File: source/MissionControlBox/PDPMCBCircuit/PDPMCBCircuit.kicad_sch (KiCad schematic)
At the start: 63 parts

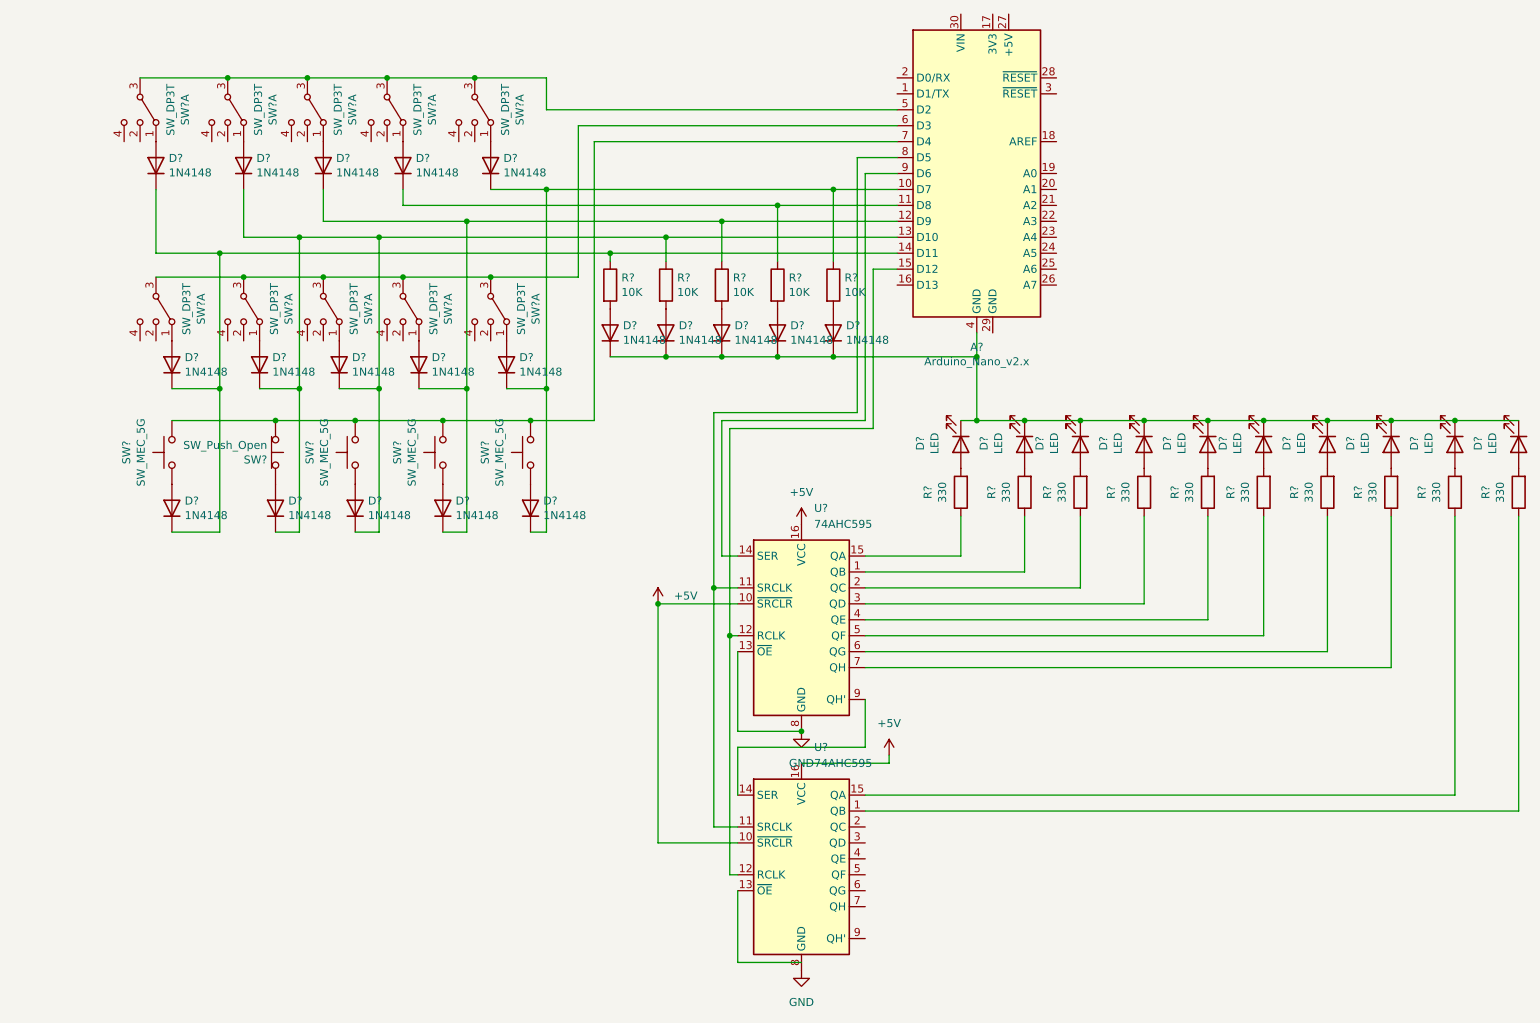
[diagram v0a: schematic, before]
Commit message: Added Labels to circuit
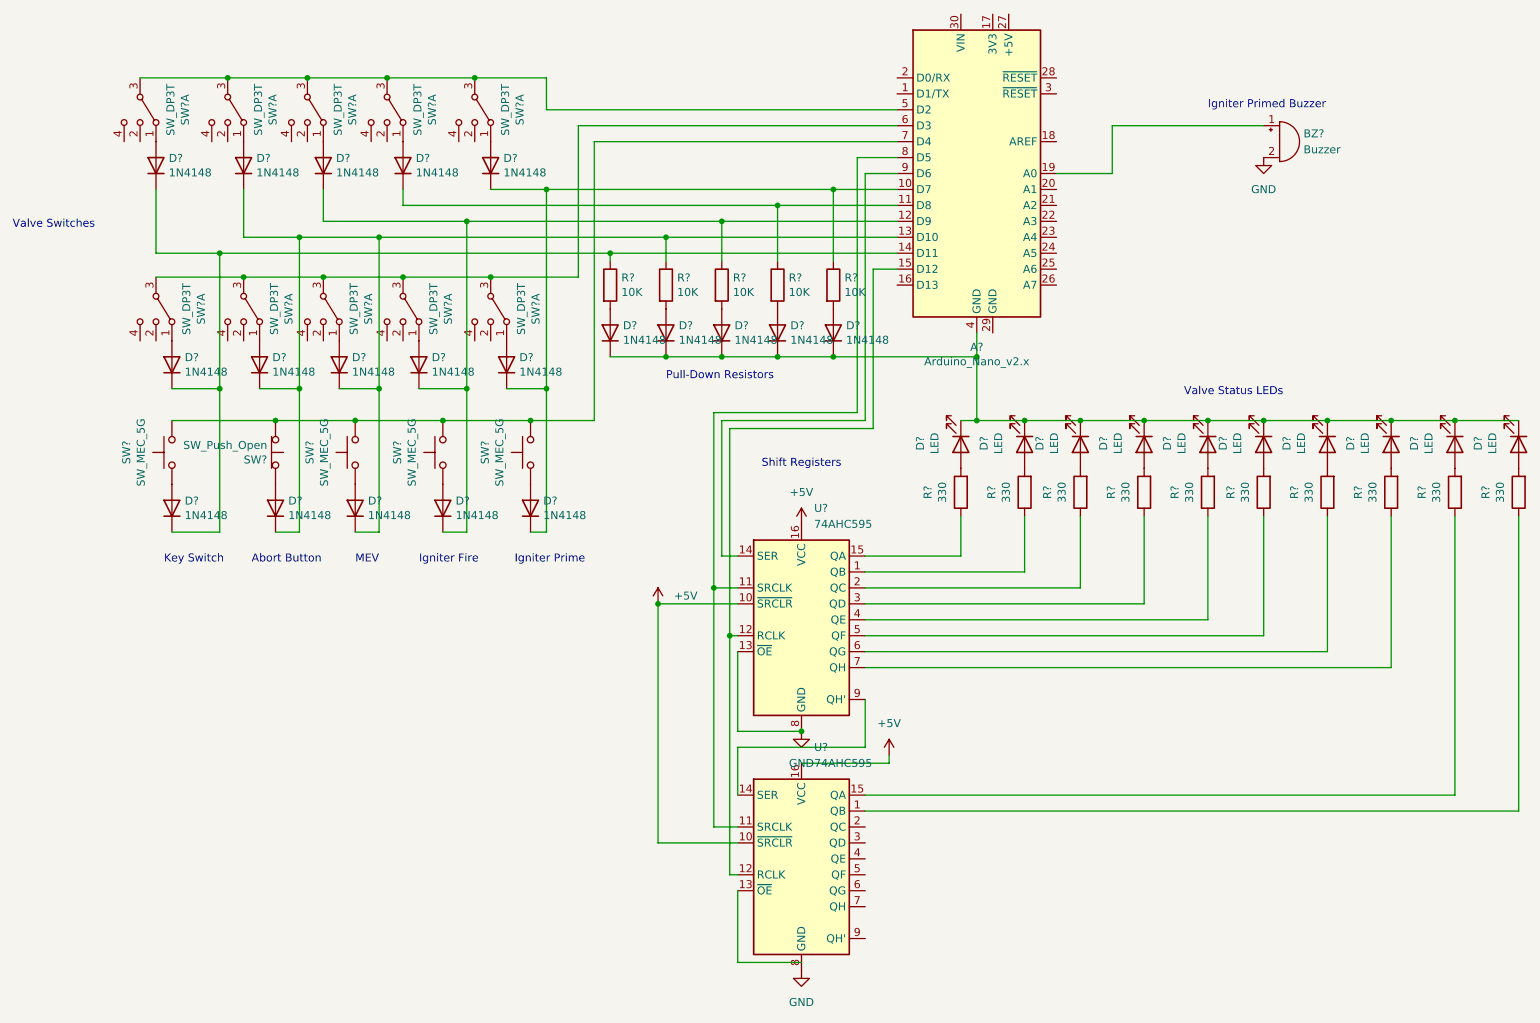
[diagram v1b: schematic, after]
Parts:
- added BZ?: Buzzer, symbol Device:Buzzer
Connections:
- net GND: now also BZ?.2 (+)
- net at A?.19 (A0): now also BZ?.1 (-)
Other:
- note added: "Abort Button"
- note added: "Igniter Fire"
- note added: "Igniter Prime"
- note added: "Igniter Primed Buzzer"
- note added: "Key Switch"
- note added: "MEV"
- note added: "Pull-Down Resistors"
- note added: "Shift Registers"
- note added: "Valve Status LEDs"
- note added: "Valve Switches"
- company: (none) -> UVic Rocketery
- title: (none) -> Propulsion Developement Platform Mission Control Box
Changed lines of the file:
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@@
 (kicad_sch (version 20211123) (generator eeschema)
   (paper "A4")
+  (title_block
+    (title "Propulsion Developement Platform Mission Control Box")
+    (date "2022-05-11")
+    (rev "R1")
+    (company "UVic Rocketery")
+  )
   (junction (at 100.33 60.96) (diameter 0) (color 0 0 0 0)
   )
@@
     (stroke (width 0) (type default) (color 0 0 0 0))
   )
+  (wire (pts (xy 203.2 53.34) (xy 203.2 45.72))
+    (stroke (width 0) (type default) (color 0 0 0 0))
+  )
   (wire (pts (xy 104.14 69.85) (xy 118.11 69.85))
     (stroke (width 0) (type default) (color 0 0 0 0))
@@
     (stroke (width 0) (type default) (color 0 0 0 0))
   )
+  (wire (pts (xy 203.2 45.72) (xy 227.33 45.72))
+    (stroke (width 0) (type default) (color 0 0 0 0))
+  )
   (wire (pts (xy 60.96 110.49) (xy 60.96 87.63))
     (stroke (width 0) (type default) (color 0 0 0 0))
@@
     (stroke (width 0) (type default) (color 0 0 0 0))
   )
+  (wire (pts (xy 194.31 53.34) (xy 203.2 53.34))
+    (stroke (width 0) (type default) (color 0 0 0 0))
+  )
   (wire (pts (xy 106.68 87.63) (xy 113.03 87.63))
     (stroke (width 0) (type default) (color 0 0 0 0))
@@
   (wire (pts (xy 247.65 92.71) (xy 237.49 92.71))
     (stroke (width 0) (type default) (color 0 0 0 0))
+  )
+  (text "Valve Switches\n" (at 27.94 62.23 0)
+    (effects (font (size 1.27 1.27)) (justify left bottom))
+  )
+  (text "MEV\n" (at 82.55 115.57 0)
+    (effects (font (size 1.27 1.27)) (justify left bottom))
+  )
+  (text "Shift Registers" (at 147.32 100.33 0)
+    (effects (font (size 1.27 1.27)) (justify left bottom))
+  )
+  (text "Abort Button" (at 66.04 115.57 0)
+    (effects (font (size 1.27 1.27)) (justify left bottom))
+  )
+  (text "Igniter Prime\n" (at 107.95 115.57 0)
+    (effects (font (size 1.27 1.27)) (justify left bottom))
+  )
+  (text "Key Switch\n" (at 52.07 115.57 0)
+    (effects (font (size 1.27 1.27)) (justify left bottom))
+  )
+  (text "Valve Status LEDs" (at 214.63 88.9 0)
+    (effects (font (size 1.27 1.27)) (justify left bottom))
+  )
+  (text "Igniter Fire\n" (at 92.71 115.57 0)
+    (effects (font (size 1.27 1.27)) (justify left bottom))
+  )
+  (text "Pull-Down Resistors" (at 132.08 86.36 0)
+    (effects (font (size 1.27 1.27)) (justify left bottom))
+  )
+  (text "Igniter Primed Buzzer" (at 218.44 43.18 0)
+    (effects (font (size 1.27 1.27)) (justify left bottom))
   )
   (symbol (lib_id "MCU_Module:Arduino_Nano_v2.x") (at 181.61 53.34 0) (unit 1)
@@
     (pin "1")
   )
+  (symbol (lib_id "Device:Buzzer") (at 229.87 48.26 0) (unit 1)
+    (in_bom yes) (on_board yes) (fields_autoplaced)
+    (property "Reference" "BZ?" (id 0) (at 233.68 46.9899 0)
+      (effects (font (size 1.27 1.27)) (justify left))
+    )
+    (property "Value" "Buzzer" (id 1) (at 233.68 49.5299 0)
+      (effects (font (size 1.27 1.27)) (justify left))
+    )
+    (property "Footprint" "" (id 2) (at 229.235 45.72 90)
+      (effects (font (size 1.27 1.27)) hide)
+    )
+    (property "Datasheet" "~" (id 3) (at 229.235 45.72 90)
+      (effects (font (size 1.27 1.27)) hide)
+    )
+    (pin "1")
+    (pin "2")
+  )
+  (symbol (lib_id "power:GND") (at 227.33 50.8 0) (unit 1)
+    (in_bom yes) (on_board yes) (fields_autoplaced)
+    (property "Reference" "#PWR?" (id 0) (at 227.33 57.15 0)
+      (effects (font (size 1.27 1.27)) hide)
+    )
+    (property "Value" "GND" (id 1) (at 227.33 55.88 0))
+    (property "Footprint" "" (id 2) (at 227.33 50.8 0)
+      (effects (font (size 1.27 1.27)) hide)
+    )
+    (property "Datasheet" "" (id 3) (at 227.33 50.8 0)
+      (effects (font (size 1.27 1.27)) hide)
+    )
+    (pin "1")
+  )
   (symbol (lib_id "power:GND") (at 153.67 180.34 0) (unit 1)
     (in_bom yes) (on_board yes) (fields_autoplaced)
@@
       (reference "#PWR?") (unit 1) (value "+5V") (footprint "")
     )
+    (path "/6185152d-bff8-4166-b2e9-7dbfdee2d5e5"
+      (reference "#PWR?") (unit 1) (value "GND") (footprint "")
+    )
     (path "/a65c7c71-5939-429e-8860-30e0f5c0e40e"
       (reference "#PWR?") (unit 1) (value "GND") (footprint "")
@@
       (reference "A?") (unit 1) (value "Arduino_Nano_v2.x") (footprint "Module:Arduino_Nano")
     )
+    (path "/4e69652b-7a91-4b21-8a76-b97415c64964"
+      (reference "BZ?") (unit 1) (value "Buzzer") (footprint "")
+    )
     (path "/00000000-0000-0000-0000-0000627aab3e"

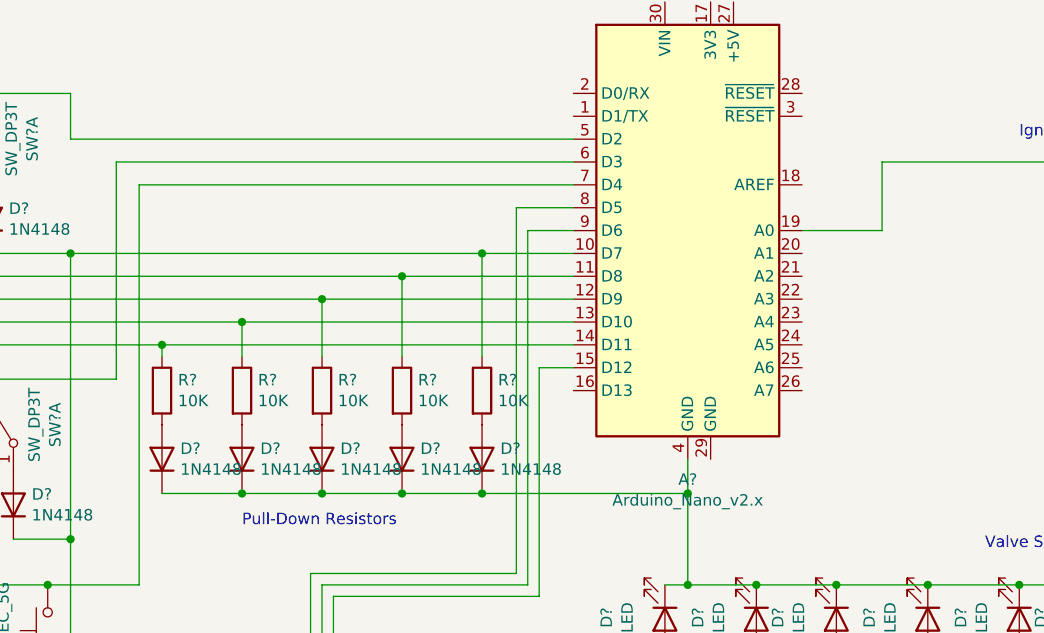
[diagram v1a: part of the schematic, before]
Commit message: commenting, compliance, schematic update
Added commenting to MCB firmware code, updated outputs for compliance with communication standard, updated schematic for adjusted circuit
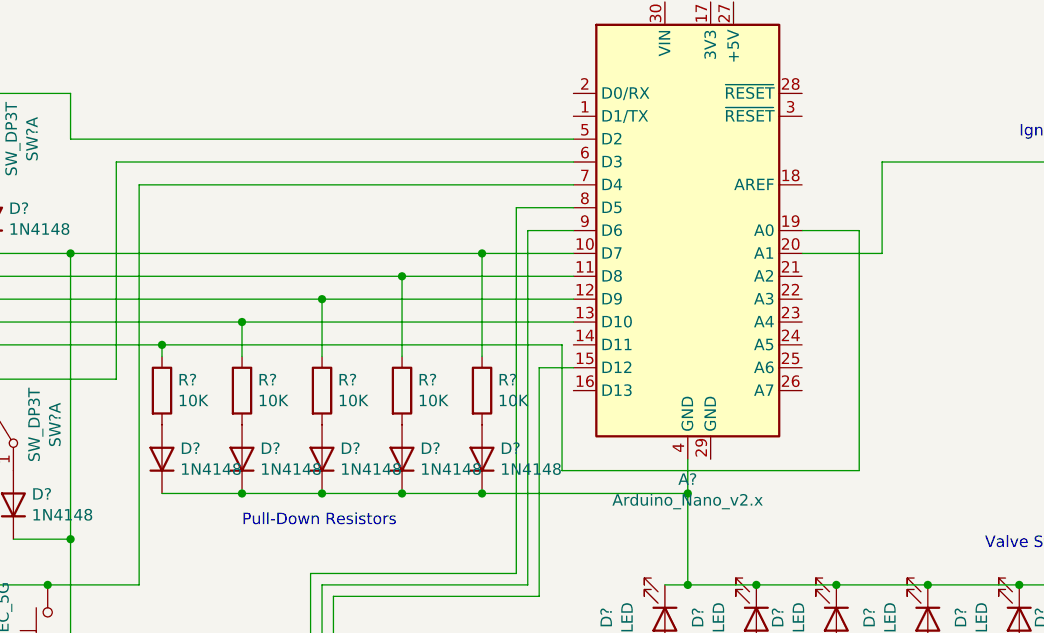
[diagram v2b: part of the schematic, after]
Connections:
- net at D?.1 (K), D?.1 (K), D?.1 (K)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: now also A?.19 (A0); no longer A?.14 (D11)
- net at BZ?.1 (-): now also A?.20 (A1); no longer A?.19 (A0)
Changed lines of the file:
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@@
     (stroke (width 0) (type default) (color 0 0 0 0))
   )
-  (wire (pts (xy 123.19 66.04) (xy 168.91 66.04))
+  (wire (pts (xy 123.19 66.04) (xy 167.64 66.04))
     (stroke (width 0) (type default) (color 0 0 0 0))
   )
@@
     (stroke (width 0) (type default) (color 0 0 0 0))
   )
-  (wire (pts (xy 203.2 53.34) (xy 203.2 45.72))
+  (wire (pts (xy 203.2 45.72) (xy 203.2 55.88))
     (stroke (width 0) (type default) (color 0 0 0 0))
   )
@@
     (stroke (width 0) (type default) (color 0 0 0 0))
   )
+  (wire (pts (xy 167.64 80.01) (xy 200.66 80.01))
+    (stroke (width 0) (type default) (color 0 0 0 0))
+  )
   (wire (pts (xy 64.77 69.85) (xy 77.47 69.85))
     (stroke (width 0) (type default) (color 0 0 0 0))
@@
     (stroke (width 0) (type default) (color 0 0 0 0))
   )
+  (wire (pts (xy 194.31 55.88) (xy 203.2 55.88))
+    (stroke (width 0) (type default) (color 0 0 0 0))
+  )
   (wire (pts (xy 96.52 92.71) (xy 110.49 92.71))
     (stroke (width 0) (type default) (color 0 0 0 0))
@@
     (stroke (width 0) (type default) (color 0 0 0 0))
   )
-  (wire (pts (xy 194.31 53.34) (xy 203.2 53.34))
+  (wire (pts (xy 194.31 53.34) (xy 200.66 53.34))
     (stroke (width 0) (type default) (color 0 0 0 0))
   )
@@
     (stroke (width 0) (type default) (color 0 0 0 0))
   )
+  (wire (pts (xy 200.66 80.01) (xy 200.66 53.34))
+    (stroke (width 0) (type default) (color 0 0 0 0))
+  )
   (wire (pts (xy 77.47 55.88) (xy 77.47 60.96))
     (stroke (width 0) (type default) (color 0 0 0 0))
@@
     (stroke (width 0) (type default) (color 0 0 0 0))
   )
+  (wire (pts (xy 167.64 66.04) (xy 167.64 80.01))
+    (stroke (width 0) (type default) (color 0 0 0 0))
+  )
